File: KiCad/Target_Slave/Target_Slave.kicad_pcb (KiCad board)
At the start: 2 copper layers, 76.2 x 50.8 mm, 44 parts, among them J1 ICSP, J2 I2C, J3 I2C, SW1 I2C Address, U1 PIC16F1788-IP, U2 TSSP4038, U3 TSOP53456

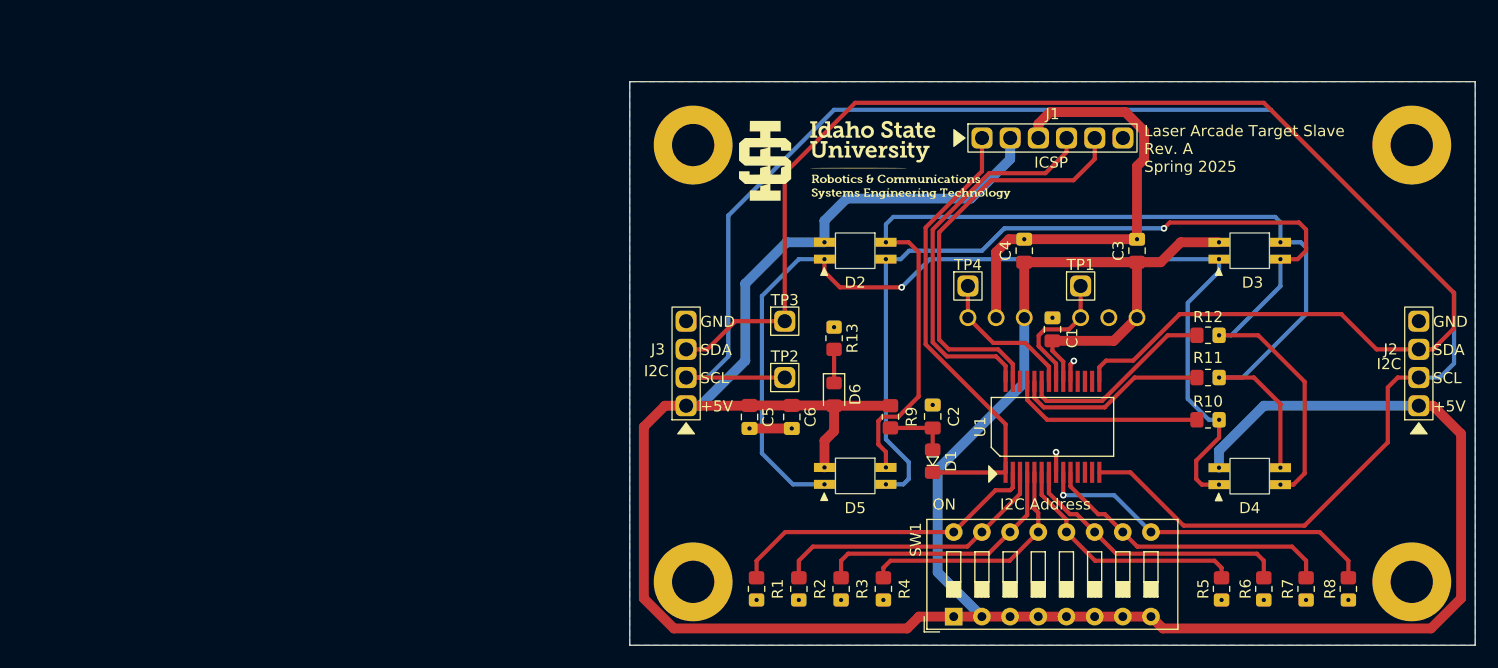
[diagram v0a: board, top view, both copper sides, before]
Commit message: Add titleblock to target PCBs
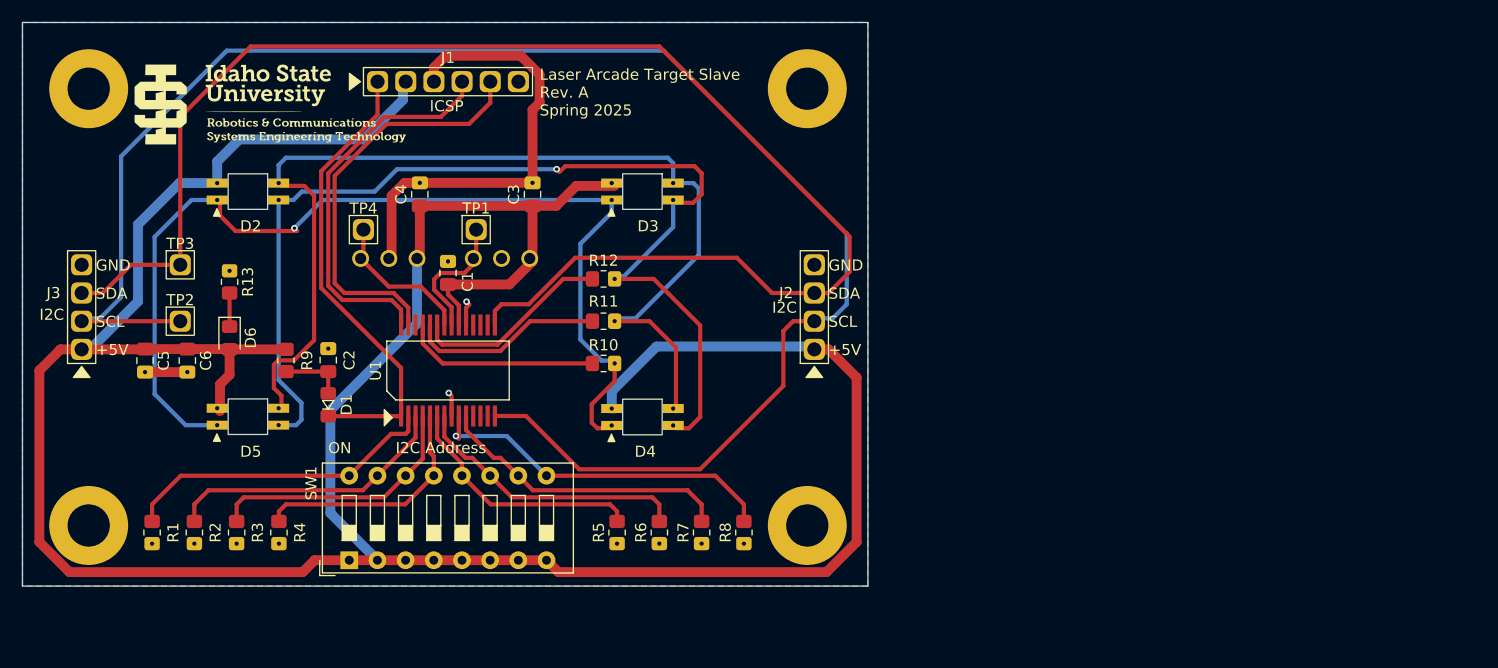
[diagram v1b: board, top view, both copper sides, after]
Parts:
- moved D3 55.0 mm to (168.8, 91.2)
- moved D4 55.0 mm to (168.8, 111.5)
- moved G*** 55.0 mm to (174.5, 102.6)
- moved G*** 55.0 mm to (121.2, 112.8)
- moved D2 55.0 mm to (133.2, 91.2)
- moved D5 55.0 mm to (133.2, 111.5)
- moved G*** 55.0 mm to (132.0, 118.1)
- moved U2 55.0 mm to (156.1, 97.2)
- moved U3 55.0 mm to (145.9, 97.2)
- moved TP2 54.7 mm to (127.1, 102.9)
- moved TP3 54.7 mm to (127.1, 97.8)
- moved ? 54.7 mm to (183.6, 121.3)
- moved C1 54.7 mm to (151.3, 98.5)
- moved C2 54.7 mm to (140.5, 106.4)
- moved C3 54.7 mm to (158.9, 91.4)
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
